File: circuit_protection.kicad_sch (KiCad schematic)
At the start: 32 parts, among them IC2 TPS16630RGER, U10 USBLC6-2SC6, U11 USBLC6-2SC6, U2 SEUC10F5V4U, U3 TPS259630DDAR, U8 USBLC6-2SC6

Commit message: updated LED resistor values
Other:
- note added: "5V Pixel Power"
- moved on the sheet: D32, F9
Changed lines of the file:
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@@
 	(rectangle
 		(start 21.336 126.238)
-		(end 115.316 193.675)
+		(end 114.3 193.04)
+		(stroke
+			(width 0.3)
+			(type solid)
+		)
+		(fill
+			(type none)
+		)
+	)
+	(rectangle
+		(start 116.84 125.73)
+		(end 171.45 193.04)
 		(stroke
 			(width 0.3)
@@
 	(rectangle
 		(start 116.84 22.86)
-		(end 171.45 154.94)
+		(end 171.45 119.38)
 		(stroke
 			(width 0.3)
@@
 		)
 	)
+	(text "5V Pixel Power"
+		(exclude_from_sim no)
+		(at 116.84 125.73 0)
+		(effects
+			(font
+				(size 3 3)
+				(thickness 0.6)
+				(bold yes)
+			)
+			(justify left bottom)
+		)
+	)
 	(text "5V Data Power"
 		(exclude_from_sim no)
@@
 	(text_box "5V logic ORing circuit. 0Ω resistors used as configurable jumpers to hard enable/disable certain power sources.\n\n+5V_FUSED (24V DC/DC output) disabled by default, but there if we want single power connector to board. Otherwise, everything just goes through a Schottky diode. There's nothing that needs a full 5V downstream, and the voltage drop should even help assure function of the addressable indicator RGB LEDs."
 		(exclude_from_sim no)
-		(at 118.745 120.015 0)
+		(at 118.11 87.63 0)
 		(size 52.705 32.385)
 		(margins 0.9525 0.9525 0.9525 0.9525)
@@
 	(text_box "Just using good old fashioned blade fuse for the high-current 5V pixel bus."
 		(exclude_from_sim no)
-		(at 117.475 181.61 0)
-		(size 56.515 12.065)
+		(at 118.11 180.34 0)
+		(size 53.34 12.065)
 		(margins 0.9525 0.9525 0.9525 0.9525)
 		(stroke
@@
 	(wire
 		(pts
-			(xy 194.31 125.73) (xy 194.31 127)
+			(xy 190.5 125.73) (xy 190.5 127)
 		)
 		(stroke
@@
 	(wire
 		(pts
-			(xy 194.31 138.43) (xy 194.31 134.62)
+			(xy 190.5 138.43) (xy 190.5 134.62)
 		)
 		(stroke
@@
 	(wire
 		(pts
-			(xy 147.32 170.18) (xy 153.67 170.18)
+			(xy 148.59 146.05) (xy 154.94 146.05)
 		)
 		(stroke
@@
 	(wire
 		(pts
-			(xy 133.35 170.18) (xy 139.7 170.18)
+			(xy 134.62 146.05) (xy 140.97 146.05)
 		)
 		(stroke
@@
 	)
 	(label "POE-"
-		(at 194.31 138.43 180)
+		(at 190.5 138.43 180)
 		(effects
 			(font
@@
 	)
 	(label "POE+"
-		(at 194.31 125.73 180)
+		(at 190.5 125.73 180)
 		(effects
 			(font
@@
 	(symbol
 		(lib_id "Diode:SMAJ24A")
-		(at 194.31 130.81 270)
+		(at 190.5 130.81 270)
 		(unit 1)
 		(exclude_from_sim no)
@@
 		(dnp no)
 		(property "Reference" "D32"
-			(at 192.024 131.318 90)
+			(at 188.214 131.318 90)
 			(effects
 				(font
@@
 		)
 		(property "Value" "SMAJ58A"
-			(at 193.294 134.112 90)
+			(at 189.484 134.112 90)
 			(effects
 				(font
@@
 		)
 		(property "Footprint" "Diode_SMD:D_SMA"
-			(at 189.23 130.81 0)
+			(at 185.42 130.81 0)
 			(effects
 				(font
@@
 		)
 		(property "Datasheet" "https://www.littelfuse.com/media?resourcetype=datasheets&itemid=75e32973-b177-4ee3-a0ff-cedaf1abdb93&filename=smaj-datasheet"
-			(at 194.31 129.54 0)
+			(at 190.5 129.54 0)
 			(effects
 				(font
@@
 		)
 		(property "Description" "400W unidirectional Transient Voltage Suppressor, 24.0Vr, SMA(DO-214AC)"
-			(at 194.31 130.81 0)
+			(at 190.5 130.81 0)
 			(effects
 				(font
@@
 		)
 		(property "LCSC" "C148235"
-			(at 194.31 130.81 0)
+			(at 190.5 130.81 0)
 			(effects
 				(font
@@
 		)
 		(property "color" ""
-			(at 194.31 130.81 0)
+			(at 190.5 130.81 0)
 			(effects
 				(font
@@
 		)
 		(property "Rating" ""
-			(at 194.31 130.81 0)
+			(at 190.5 130.81 0)
 			(effects
 				(font
@@
 	(symbol
 		(lib_id "power:+5V")
-		(at 153.67 170.18 0)
+		(at 154.94 146.05 0)
 		(unit 1)
 		(exclude_from_sim no)
@@
 		(fields_autoplaced yes)
 		(property "Reference" "#PWR062"
-			(at 153.67 173.99 0)
+			(at 154.94 149.86 0)
 			(effects
 				(font
@@
 		)
 		(property "Value" "+5V_PS"
-			(at 156.21 168.9099 0)
+			(at 157.48 144.7799 0)
 			(effects
 				(font
@@
 		)
 		(property "Footprint" ""
-			(at 153.67 170.18 0)
+			(at 154.94 146.05 0)
 			(effects
 				(font
@@
 		)
 		(property "Datasheet" ""
-			(at 153.67 170.18 0)
+			(at 154.94 146.05 0)
 			(effects
 				(font
@@
 		)
 		(property "Description" "Power symbol creates a global label with name \"+5V\""
-			(at 153.67 170.18 0)
+			(at 154.94 146.05 0)
 			(effects
 				(font
@@
 		)
 		(property "LCSC" ""
-			(at 153.67 170.18 0)
+			(at 154.94 146.05 0)
 			(effects
 				(font
@@
 	(symbol
 		(lib_id "Device:Fuse")
-		(at 143.51 170.18 90)
+		(at 144.78 146.05 90)
 		(unit 1)
 		(exclude_from_sim no)
@@
 		(fields_autoplaced yes)
 		(property "Reference" "F9"
-			(at 142.2978 168.656 0)
+			(at 143.5678 144.526 0)
 			(effects
 				(font
@@
 		)
 		(property "Value" "Fuse 20A"
-			(at 144.7221 168.656 0)
+			(at 145.9921 144.526 0)
 			(effects
 				(font
@@
 		)
 		(property "Footprint" "easyeda2kicad:FUSE-TH_4P-L16.0-W6.7"
-			(at 143.51 171.958 90)
+			(at 144.78 147.828 90)
 			(effects
 				(font
@@
 		)
 		(property "Datasheet" "~"
-			(at 143.51 170.18 0)
+			(at 144.78 146.05 0)
 			(effects
 				(font
@@
 		)
 		(property "Description" "Fuse"
-			(at 143.51 170.18 0)
+			(at 144.78 146.05 0)
 			(effects
 				(font
@@
 		)
 		(property "LCSC" "C19727305"
-			(at 143.51 170.18 0)
+			(at 144.78 146.05 0)
 			(effects
 				(font
@@
 		)
 		(property "color" ""
-			(at 143.51 170.18 0)
+			(at 144.78 146.05 0)
 			(effects
 				(font
@@
 		)
 		(property "Availability" ""
-			(at 143.51 170.18 0)
+			(at 144.78 146.05 0)
 			(effects
 				(font
@@
 		)
 		(property "Check_prices" ""
-			(at 143.51 170.18 0)
+			(at 144.78 146.05 0)
 			(effects
 				(font
@@
 		)
 		(property "Description_1" ""
-			(at 143.51 170.18 0)
+			(at 144.78 146.05 0)
 			(effects
 				(font
@@
 		)
 		(property "MANUFACTURER" ""
-			(at 143.51 170.18 0)
+			(at 144.78 146.05 0)
 			(effects
 				(font
@@
 		)
 		(property "MAXIMUM_PACKAGE_HEIGHT" ""
-			(at 143.51 170.18 0)
+			(at 144.78 146.05 0)
 			(effects
 				(font
@@
 		)
 		(property "MF" ""
-			(at 143.51 170.18 0)
+			(at 144.78 146.05 0)
 			(effects
 				(font
@@
 		)
 		(property "MP" ""
-			(at 143.51 170.18 0)
+			(at 144.78 146.05 0)
 			(effects
 				(font
@@
 		)
 		(property "PARTREV" ""
-			(at 143.51 170.18 0)
+			(at 144.78 146.05 0)
 			(effects
 				(font
@@
 		)
 		(property "Package" ""
-			(at 143.51 170.18 0)
+			(at 144.78 146.05 0)
 			(effects
 				(font
@@
 		)
 		(property "Price" ""
-			(at 143.51 170.18 0)
+			(at 144.78 146.05 0)
 			(effects
 				(font
@@
 		)
 		(property "SNAPEDA_PN" ""
-			(at 143.51 170.18 0)
+			(at 144.78 146.05 0)
 			(effects
 				(font
@@
 		)
 		(property "STANDARD" ""
-			(at 143.51 170.18 0)
+			(at 144.78 146.05 0)
 			(effects
 				(font
@@
 		)
 		(property "SnapEDA_Link" ""
-			(at 143.51 170.18 0)
+			(at 144.78 146.05 0)
 			(effects
 				(font
@@
 		)
 		(property "Rating" ""
-			(at 143.51 170.18 0)
+			(at 144.78 146.05 0)
 			(effects
 				(font
@@
 	(symbol
 		(lib_id "power:+5V")
-		(at 133.35 170.18 0)
+		(at 134.62 146.05 0)
 		(unit 1)
 		(exclude_from_sim no)
@@
 		(dnp no)
 		(property "Reference" "#PWR06"
-			(at 133.35 173.99 0)
+			(at 134.62 149.86 0)
 			(effects
 				(font
@@
 		)
 		(property "Value" "+5V_FUSED"
-			(at 120.396 168.91 0)
+			(at 121.666 144.78 0)
 			(effects
 				(font
@@
 		)
 		(property "Footprint" ""
-			(at 133.35 170.18 0)
+			(at 134.62 146.05 0)
 			(effects
 				(font
@@
 		)
 		(property "Datasheet" ""
-			(at 133.35 170.18 0)
+			(at 134.62 146.05 0)
 			(effects
 				(font
@@
 		)
 		(property "Description" "Power symbol creates a global label with name \"+5V\""
-			(at 133.35 170.18 0)
+			(at 134.62 146.05 0)
 			(effects
 				(font
@@
 		)
 		(property "LCSC" ""
-			(at 133.35 170.18 0)
+			(at 134.62 146.05 0)
 			(effects
 				(font

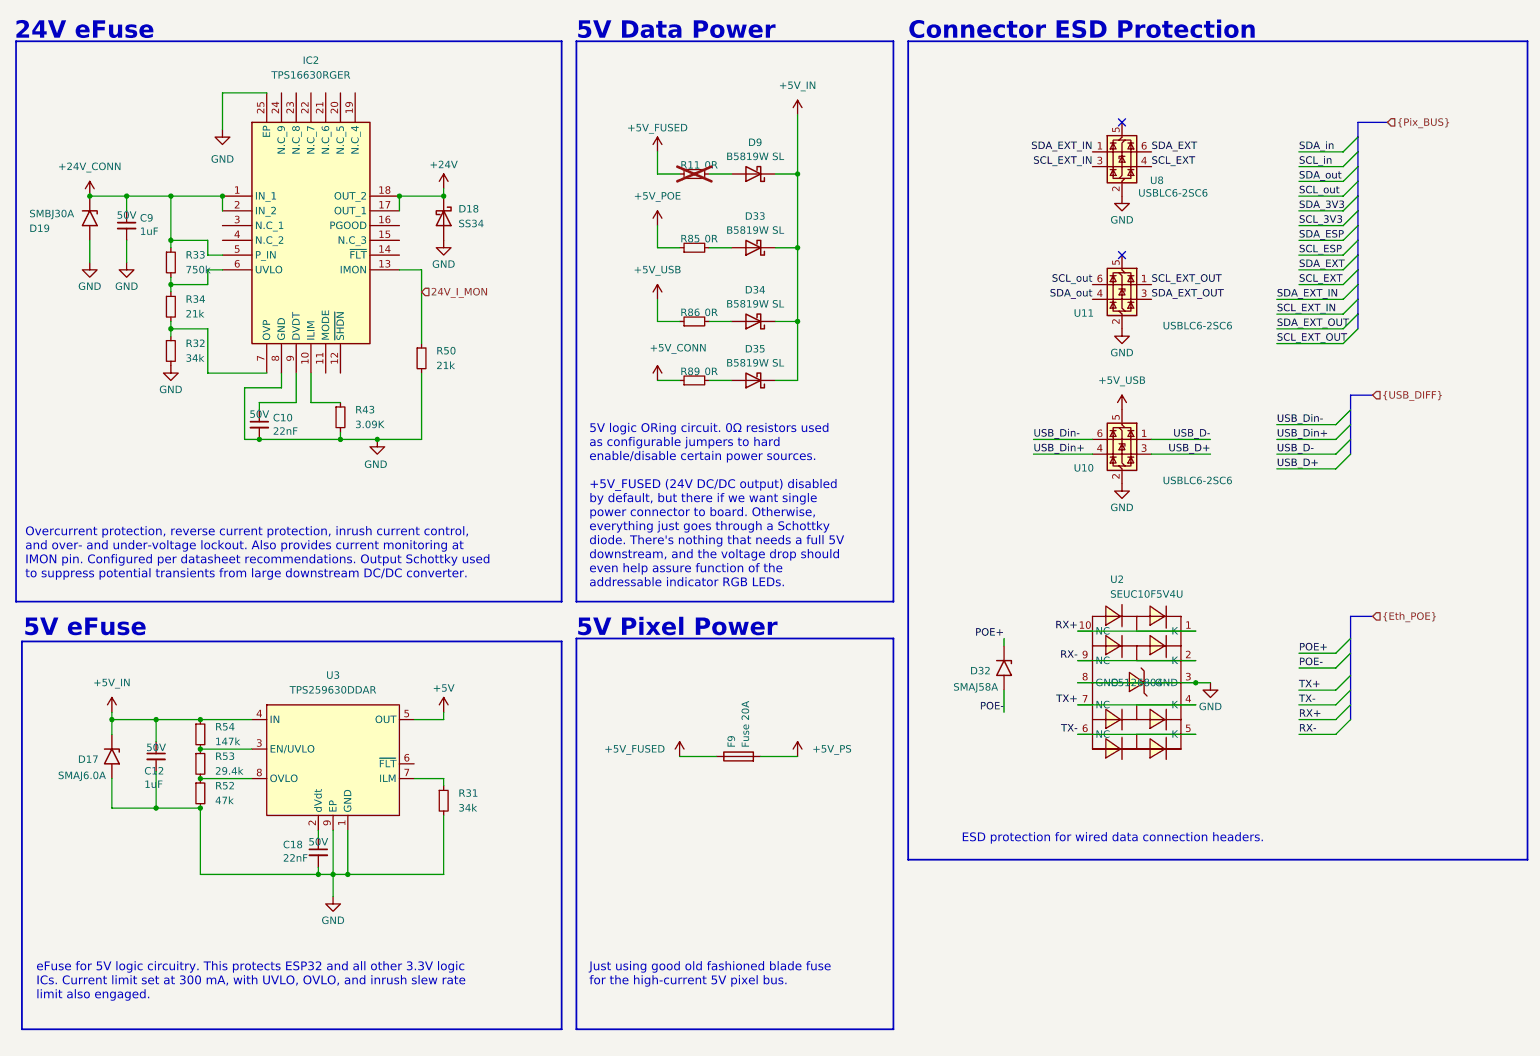
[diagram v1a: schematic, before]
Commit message: Changed 24V eFuse to TPS26632 and added reverse polarity protection
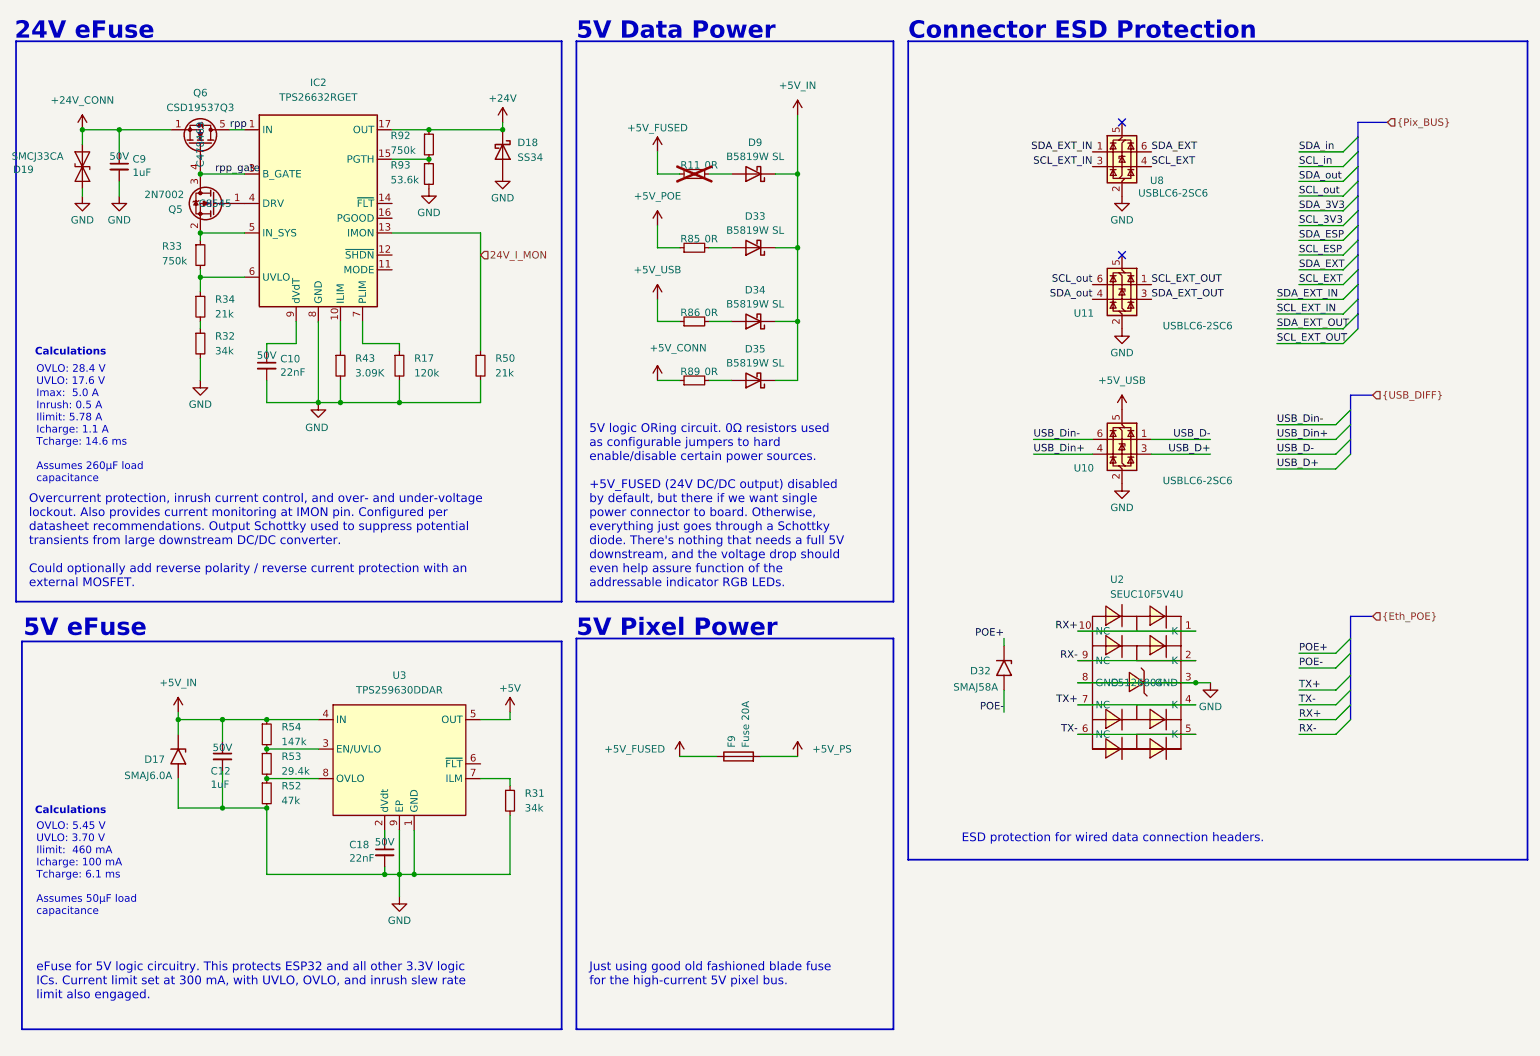
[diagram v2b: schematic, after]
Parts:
- added Q5: 2N7002, Package_TO_SOT_SMD:SOT-23, symbol Transistor_FET:2N7002
- added Q6: CSD19537Q3, Package_SON:VSON-8_3.3x3.3mm_P0.65mm_NexFET, symbol Transistor_FET:CSD19537Q3
- added R17: 120k, Resistor_SMD:R_0603_1608Metric, symbol Device:R_Small
- added R92: 750k, Resistor_SMD:R_0603_1608Metric, symbol Device:R_Small
- added R93: 53.6k, Resistor_SMD:R_0603_1608Metric, symbol Device:R_Small
- D19: value SMBJ30A -> SMCJ33CA; footprint Diode_SMD:D_SMB -> Diode_SMD:D_SMA; symbol Diode:SMAJ24A -> Diode:SMAJ5.0CA; LCSC C224017 -> C224050
- IC2: value TPS16630RGER -> TPS26632RGET; footprint Package_DFN_QFN:VQFN-24-1EP_4x4mm_P0.5mm_EP2.45x2.45mm -> Package_DFN_QFN:Texas_RGE0024H_VQFN-24-1EP_4x4mm_P0.5mm_EP2.7x2.7mm_ThermalVias; symbol Power_Protection:TPS16630RGER -> Power_Management:TPS26632RGE; LCSC C1850279 -> C2862529; Manufacturer_Part_Number TPS16630RGER -> TPS26632RGET; Mouser Part Number 595-TPS16630RGER -> (none); Mouser Price/Stock https://www.mouser.co.uk/ProductDetail/Texas-Instruments/TP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 -> (none)
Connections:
- net +24V: now also R92.1
- net +24V_CONN: now also Q6.1 (S), Q6.2 (S), Q6.3 (S); no longer IC2.1 (IN_1), IC2.2 (IN_2), IC2.5 (P_IN), R33.1
- net GND: now also R17.2, R93.2
- net at R32.1, R34.2: no longer IC2.7 (OVP)
- net at IC2.15 (PGTH): now also R92.2, R93.1
- net rpp_gate: now reaches IC2.3 (B_GATE)
- net rpp_gate: now also Q5.3 (D), Q6.4 (G)
- net at IC2.4 (DRV): now also Q5.1 (G)
- new net: IC2.5 (IN_SYS), Q5.2 (S), R33.1
- new net: IC2.7 (PLIM), R17.1
- new net rpp: IC2.1 (IN), IC2.2 (IN), Q6.5 (D)
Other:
- note added: "Calculations"
- moved on the sheet: C10, C12, C18, C9, D17, D18, R31, R32, R33, R34, R43, R50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
